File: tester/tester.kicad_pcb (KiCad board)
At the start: 4 copper layers, 150 x 120 mm, 139 parts, among them J101 X1, J102 X3, J103 X2, J201 PWR, J202 SWD, J306 DISP, J307 SD-Card, J401 USB_B_Micro, Q201 SI2301CDS-T1-GE3, SW201 Reset, SW301 SW_Push, SW302 SW_Push, SW303 SW_Push, SW304 SW_Push, SW305 SW_Push, U101 PCA9539xPW, U102 PCA9539xPW, U201 AMS1117-3.3, U202 STM32F103C8Tx, U203 M24C64-RMN, U204 M24C64-RMN, U401 USBLC6-2SC6, U402 XC6206P332MR, U403 CH340N, Y201 8MHz, Y202 32k

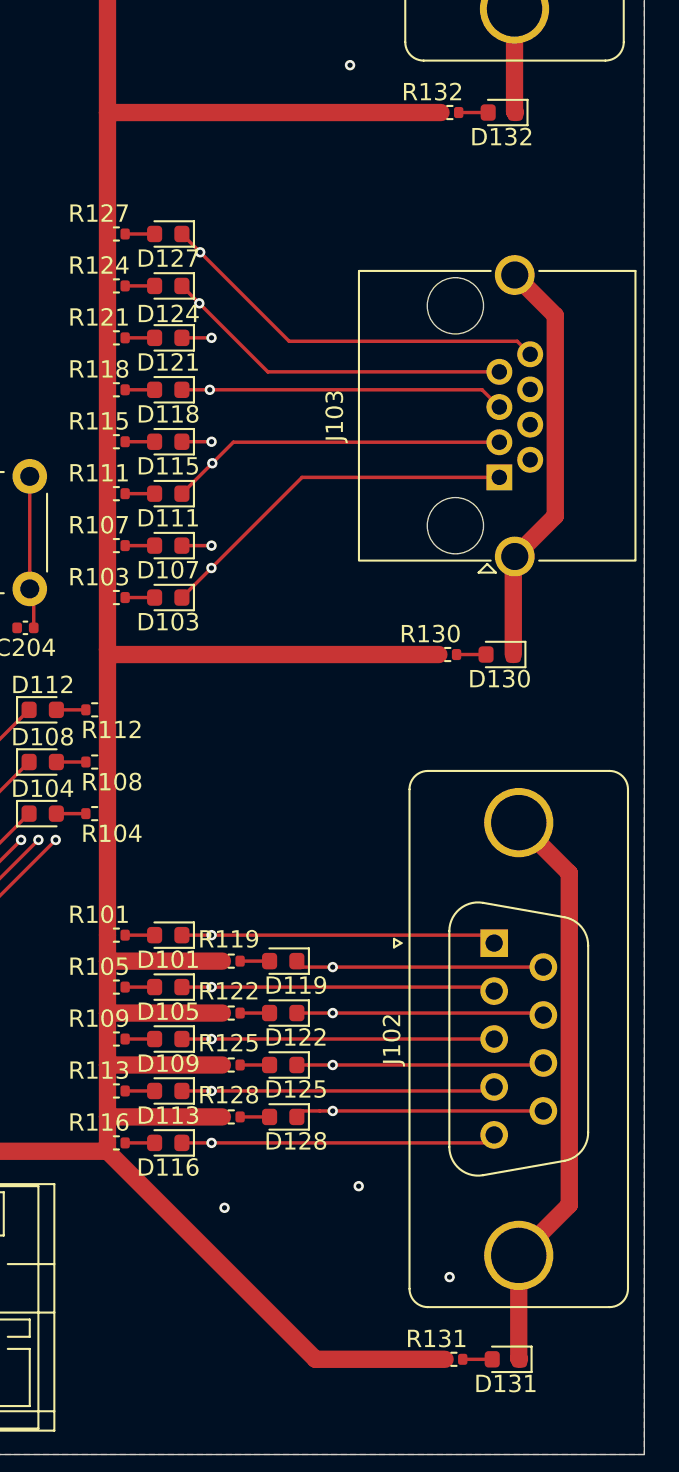
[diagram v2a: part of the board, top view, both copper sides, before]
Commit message: Rework RJ45 connector
Signed-off-by: Benedikt Spranger <b.spranger@linutronix.de>
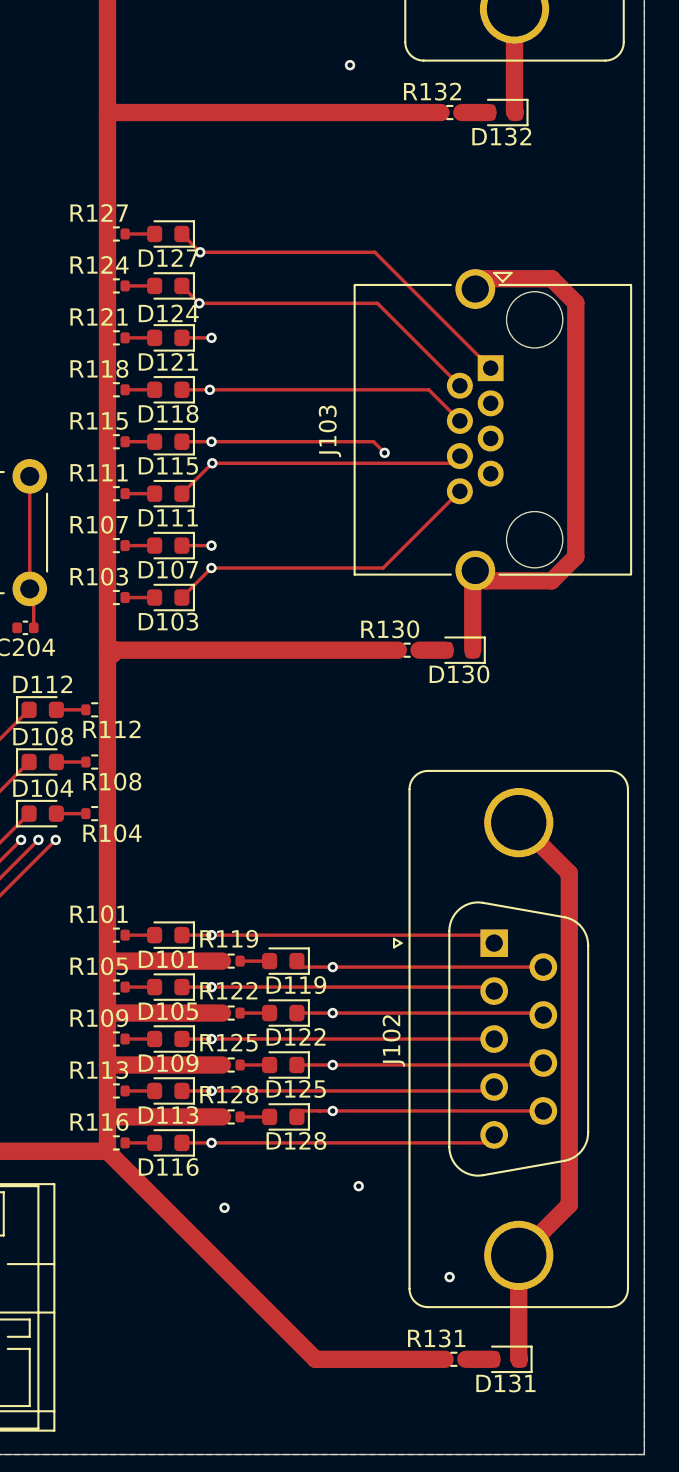
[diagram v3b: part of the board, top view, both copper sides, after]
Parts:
- moved J103 6.33 mm to (256.1, 82.2), turned to -90 degrees
- moved D130 2.36 mm to (254.3, 98.5)
- moved R130 2.36 mm to (251.3, 98.5)
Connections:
- D103 pad 1: /R1 -> /R8
- D107 pad 1: /R2 -> /R7
- D111 pad 1: /R3 -> /R6
- D115 pad 1: /R4 -> /R5
- D118 pad 1: /R5 -> /R4
- D121 pad 1: /R6 -> /R3
- D124 pad 1: /R7 -> /R2
- D127 pad 1: /R8 -> /R1
- U101 pad 13: /R1 -> /R8
- U101 pad 14: /R2 -> /R7
- U101 pad 15: /R3 -> /R6
- U101 pad 16: /R4 -> /R5
- U101 pad 17: /R5 -> /R4
- U101 pad 18: /R6 -> /R3
- U101 pad 19: /R7 -> /R2
- U101 pad 20: /R8 -> /R1
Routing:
- net /R2: track 57.3 -> 41.0 mm
- net /R1: track 56.5 -> 41.5 mm
- net /R4: track 54.7 -> 43.4 mm
- net /R7: track 43.0 -> 54.0 mm
- net /R8: track 43.4 -> 53.9 mm
- net /R5: track 45.4 -> 52.7 mm, vias 2 -> 3
- net /RSH: track 67.1 -> 73.3 mm
- net /R6: track 49.3 -> 46.8 mm
- net +5V: track 236.6 -> 234.4 mm
- net /R3: track 49.4 -> 47.7 mm
- net /MSH: track 109.6 -> 108.3 mm

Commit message: Fix SWD
Signed-off-by: Benedikt Spranger <b.spranger@linutronix.de>
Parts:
- moved C214 0.79 mm to (206.2, 97.0), turned to 0 degrees
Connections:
- U202 pad 25: unconnected-(U202-PB12-Pad25) -> /MCU/~{RST1}
- U202 pad 34: /MCU/~{RST1} -> /MCU/SYS_SWDIO
- U202 pad 38: /MCU/SYS_SWDIO -> unconnected-(U202-PA15-Pad38)
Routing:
- net /MCU/~{RST1}: track 40.9 -> 45.4 mm
- net /MCU/SYS_SWDIO: track 17.0 -> 14.1 mm
- net /MCU/SYS_SWCLK: track 12.5 -> 14.1 mm
- net /MCU/SPI2_MISO: track 100.1 -> 98.5 mm
- net +3V3: track 70.8 -> 71.4 mm
- net /R6: track 46.8 -> 46.2 mm

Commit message: Add missing I2C pullups
Signed-off-by: Benedikt Spranger <b.spranger@linutronix.de>
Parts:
- added R207: 4k7, Resistor_SMD:R_0402_1005Metric, F.Cu at (205.0, 115.5)
- added R208: 4k7, Resistor_SMD:R_0402_1005Metric, F.Cu at (203.8, 115.5)
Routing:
- net /MCU/I2C2_SCL: track 13.0 -> 18.6 mm
- net /MCU/I2C2_SDA: track 13.0 -> 14.8 mm
- net +3V3: track 71.4 -> 73.2 mm, vias 11 -> 12

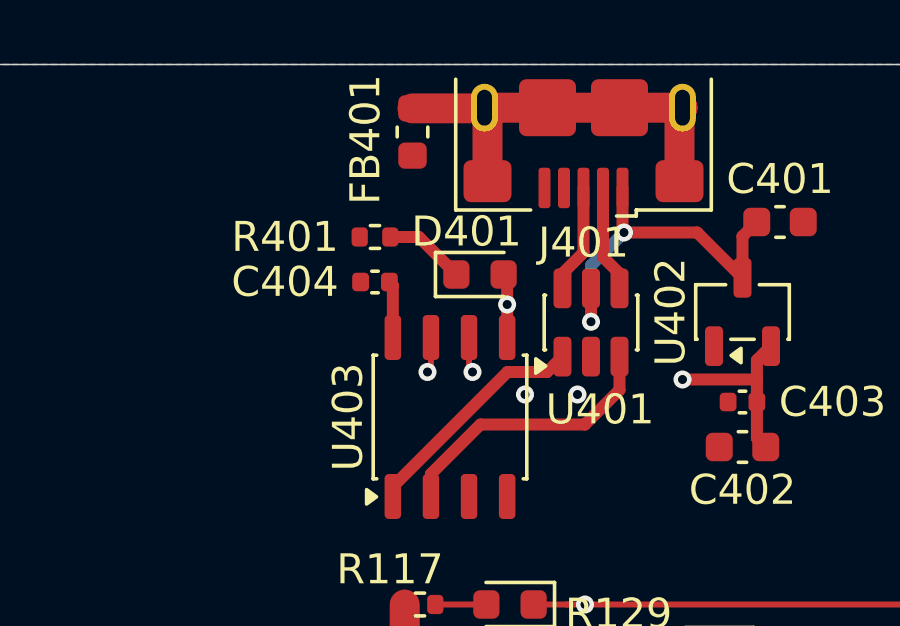
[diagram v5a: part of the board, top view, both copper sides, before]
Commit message: Enable CH340N 3.3V operation
Signed-off-by: Benedikt Spranger <b.spranger@linutronix.de>
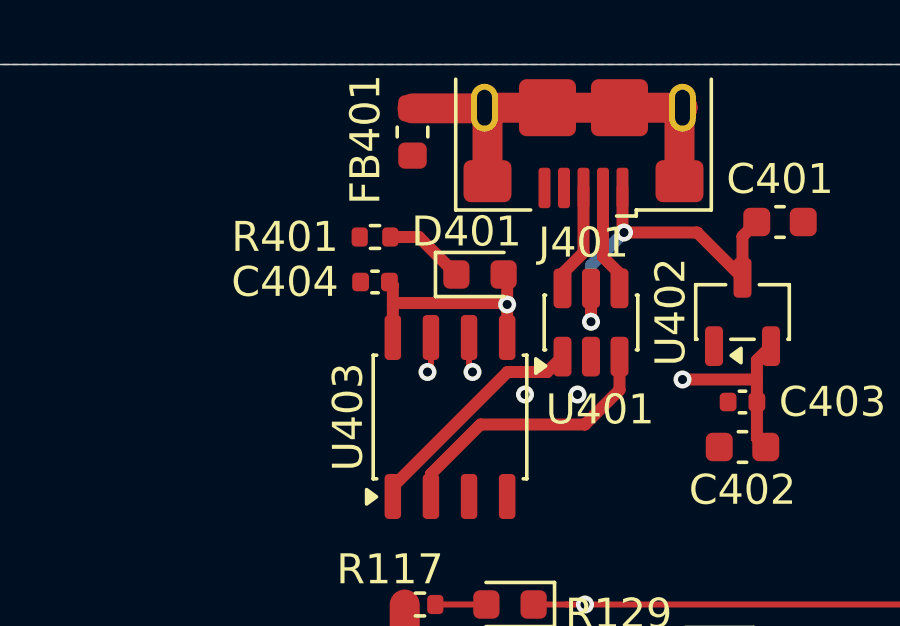
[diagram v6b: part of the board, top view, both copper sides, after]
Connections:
- C404 pad 1: Net-(U403-V3) -> Net-(D401-A)
- U403 pad 8: Net-(U403-V3) -> Net-(D401-A)
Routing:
- net Net-(D401-A): track 15.0 -> 20.8 mm
- net Net-(U403-V3): track 1.90 -> 0.00 mm
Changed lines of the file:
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@@
 			(layers "F.Cu" "F.Mask" "F.Paste")
 			(roundrect_rratio 0.25)
-			(net "Net-(U403-V3)")
+			(net "Net-(D401-A)")
 			(pintype "passive")
 		)
@@
 			(layers "F.Cu" "F.Mask" "F.Paste")
 			(roundrect_rratio 0.25)
-			(net "Net-(U403-V3)")
+			(net "Net-(D401-A)")
 			(pinfunction "V3_8")
 			(pintype "passive")
@@
 	)
 	(segment
+		(start 233.595 32.365)
+		(end 233.48 32.25)
+		(width 0.4)
+		(layer "F.Cu")
+		(net "Net-(D401-A)")
+	)
+	(segment
 		(start 245.73 36.25)
 		(end 245.73 37.455)
@@
 	)
 	(segment
+		(start 233.595 34.1)
+		(end 233.595 33)
+		(width 0.4)
+		(layer "F.Cu")
+		(net "Net-(D401-A)")
+	)
+	(segment
 		(start 245.73 35.5)
 		(end 245.73 34.8575)
@@
 	)
 	(segment
+		(start 233.595 33)
+		(end 233.595 32.365)
+		(width 0.4)
+		(layer "F.Cu")
+		(net "Net-(D401-A)")
+	)
+	(segment
+		(start 233.645 32.95)
+		(end 233.595 33)
+		(width 0.4)
+		(layer "F.Cu")
+		(net "Net-(D401-A)")
+	)
+	(segment
 		(start 245.73 37.455)
 		(end 246.025 37.75)
@@
 	)
 	(segment
+		(start 237.405 33)
+		(end 237.355 32.95)
+		(width 0.4)
+		(layer "F.Cu")
+		(net "Net-(D401-A)")
+	)
+	(segment
 		(start 237.405 34.1)
 		(end 237.405 33)
@@
 		(net "Net-(D401-A)")
 	)
+	(segment
+		(start 237.355 32.95)
+		(end 233.645 32.95)
+		(width 0.4)
+		(layer "F.Cu")
+		(net "Net-(D401-A)")
+	)
 	(via
 		(at 237.405 33)
@@
 	)
 	(segment
+		(start 205 116.055)
+		(end 203.255 117.8)
+		(width 0.2)
+		(layer "F.Cu")
+		(net "/MCU/I2C2_SCL")
+	)
+	(segment
+		(start 201.25 104.1625)
+		(end 201.25 108.41)
+		(width 0.2)
+		(layer "F.Cu")
+		(net "/MCU/I2C2_SCL")
+	)
+	(segment
+		(start 200.885 116.870552)
+		(end 200.885 116.525)
+		(width 0.2)
+		(layer "F.Cu")
+		(net "/MCU/I2C2_SCL")
+	)
+	(segment
+		(start 203.255 117.8)
+		(end 201.814448 117.8)
+		(width 0.2)
+		(layer "F.Cu")
+		(net "/MCU/I2C2_SCL")
+	)
+	(segment
+		(start 201.814448 117.8)
+		(end 200.885 116.870552)
+		(width 0.2)
+		(layer "F.Cu")
+		(net "/MCU/I2C2_SCL")
+	)
+	(segment
+		(start 200.25 109.41)
+		(end 200.25 115.89)
+		(width 0.2)
+		(layer "F.Cu")
+		(net "/MCU/I2C2_SCL")
+	)
+	(segment
+		(start 201.25 108.41)
+		(end 200.885 108.775)
+		(width 0.2)
+		(layer "F.Cu")
+		(net "/MCU/I2C2_SCL")
+	)
+	(segment
+		(start 200.885 108.775)
+		(end 200.25 109.41)
+		(width 0.2)
+		(layer "F.Cu")
+		(net "/MCU/I2C2_SCL")
+	)
+	(segment
+		(start 200.25 115.89)
+		(end 200.885 116.525)
+		(width 0.2)
+		(layer "F.Cu")
+		(net "/MCU/I2C2_SCL")
+	)
+	(segment
 		(start 224.425 115.425)
 		(end 225 116)
@@
 	)
 	(segment
+		(start 201.75 108.37)
+		(end 202.155 108.775)
+		(width 0.2)
+		(layer "F.Cu")
+		(net "/MCU/I2C2_SDA")
+	)
+	(segment
+		(start 201.75 104.1625)
+		(end 201.75 108.37)
+		(width 0.2)
+		(layer "F.Cu")
+		(net "/MCU/I2C2_SDA")
+	)
+	(segment
+		(start 203.295 116.525)
+		(end 203.765 116.055)
+		(width 0.2)
+		(layer "F.Cu")
+		(net "/MCU/I2C2_SDA")
+	)
+	(segment
+		(start 201.555 109.375)
+		(end 201.555 115.925)
+		(width 0.2)
+		(layer "F.Cu")
+		(net "/MCU/I2C2_SDA")
+	)
+	(segment
+		(start 201.555 115.925)
+		(end 202.155 116.525)
+		(width 0.2)
+		(layer "F.Cu")
+		(net "/MCU/I2C2_SDA")
+	)
+	(segment
+		(start 202.155 116.525)
+		(end 203.295 116.525)
+		(width 0.2)
+		(layer "F.Cu")
+		(net "/MCU/I2C2_SDA")
+	)
+	(segment
+		(start 202.155 108.775)
+		(end 201.555 109.375)
+		(width 0.2)
+		(layer "F.Cu")
+		(net "/MCU/I2C2_SDA")
+	)
+	(segment
 		(start 221.974999 71.825)
 		(end 222.275 72.125001)
@@
 	)
 	(segment
-		(start 233.595 32.365)
-		(end 233.48 32.25)
-		(width 0.4)
-		(layer "F.Cu")
-		(net "Net-(U403-V3)")
-	)
-	(segment
-		(start 233.595 34.1)
-		(end 233.595 32.365)
-		(width 0.4)
-		(layer "F.Cu")
-		(net "Net-(U403-V3)")
-	)
-	(segment
 		(start 229.73 97.25)
 		(end 229.73 95.23)
@@
 	)
 	(segment
-		(start 201.75 108.37)
-		(end 202.155 108.775)
-		(width 0.2)
-		(layer "F.Cu")
-		(net "/MCU/I2C2_SDA")
-	)
-	(segment
-		(start 201.75 104.1625)
-		(end 201.75 108.37)
-		(width 0.2)
-		(layer "F.Cu")
-		(net "/MCU/I2C2_SDA")
-	)
-	(segment
-		(start 203.295 116.525)
-		(end 203.765 116.055)
-		(width 0.2)
-		(layer "F.Cu")
-		(net "/MCU/I2C2_SDA")
-	)
-	(segment
-		(start 201.555 109.375)
-		(end 201.555 115.925)
-		(width 0.2)
-		(layer "F.Cu")
-		(net "/MCU/I2C2_SDA")
-	)
-	(segment
-		(start 201.555 115.925)
-		(end 202.155 116.525)
-		(width 0.2)
-		(layer "F.Cu")
-		(net "/MCU/I2C2_SDA")
-	)
-	(segment
-		(start 202.155 116.525)
-		(end 203.295 116.525)
-		(width 0.2)
-		(layer "F.Cu")
-		(net "/MCU/I2C2_SDA")
-	)
-	(segment
-		(start 202.155 108.775)
-		(end 201.555 109.375)
-		(width 0.2)
-		(layer "F.Cu")
-		(net "/MCU/I2C2_SDA")
-	)
-	(segment
-		(start 205 116.055)
-		(end 203.255 117.8)
-		(width 0.2)
-		(layer "F.Cu")
-		(net "/MCU/I2C2_SCL")
-	)
-	(segment
-		(start 201.25 104.1625)
-		(end 201.25 108.41)
-		(width 0.2)
-		(layer "F.Cu")
-		(net "/MCU/I2C2_SCL")
-	)
-	(segment
-		(start 200.885 116.870552)
-		(end 200.885 116.525)
-		(width 0.2)
-		(layer "F.Cu")
-		(net "/MCU/I2C2_SCL")
-	)
-	(segment
-		(start 203.255 117.8)
-		(end 201.814448 117.8)
-		(width 0.2)
-		(layer "F.Cu")
-		(net "/MCU/I2C2_SCL")
-	)
-	(segment
-		(start 201.814448 117.8)
-		(end 200.885 116.870552)
-		(width 0.2)
-		(layer "F.Cu")
-		(net "/MCU/I2C2_SCL")
-	)
-	(segment
-		(start 200.25 109.41)
-		(end 200.25 115.89)
-		(width 0.2)
-		(layer "F.Cu")
-		(net "/MCU/I2C2_SCL")
-	)
-	(segment
-		(start 201.25 108.41)
-		(end 200.885 108.775)
-		(width 0.2)
-		(layer "F.Cu")
-		(net "/MCU/I2C2_SCL")
-	)
-	(segment
-		(start 200.885 108.775)
-		(end 200.25 109.41)
-		(width 0.2)
-		(layer "F.Cu")
-		(net "/MCU/I2C2_SCL")
-	)
-	(segment
-		(start 200.25 115.89)
-		(end 200.885 116.525)
-		(width 0.2)
-		(layer "F.Cu")
-		(net "/MCU/I2C2_SCL")
-	)
-	(segment

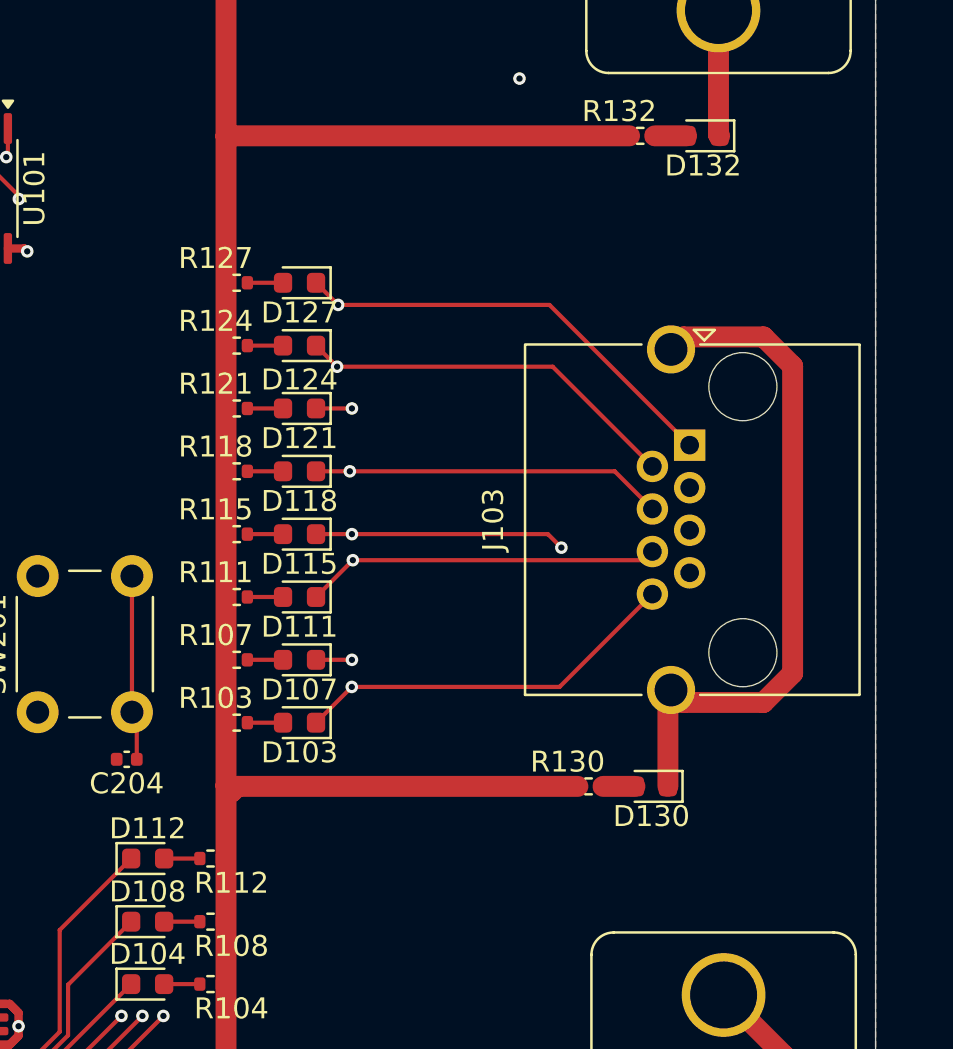
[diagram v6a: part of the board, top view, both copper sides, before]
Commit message: Use RJ45 connector with LEDs
Signed-off-by: Benedikt Spranger <b.spranger@linutronix.de>
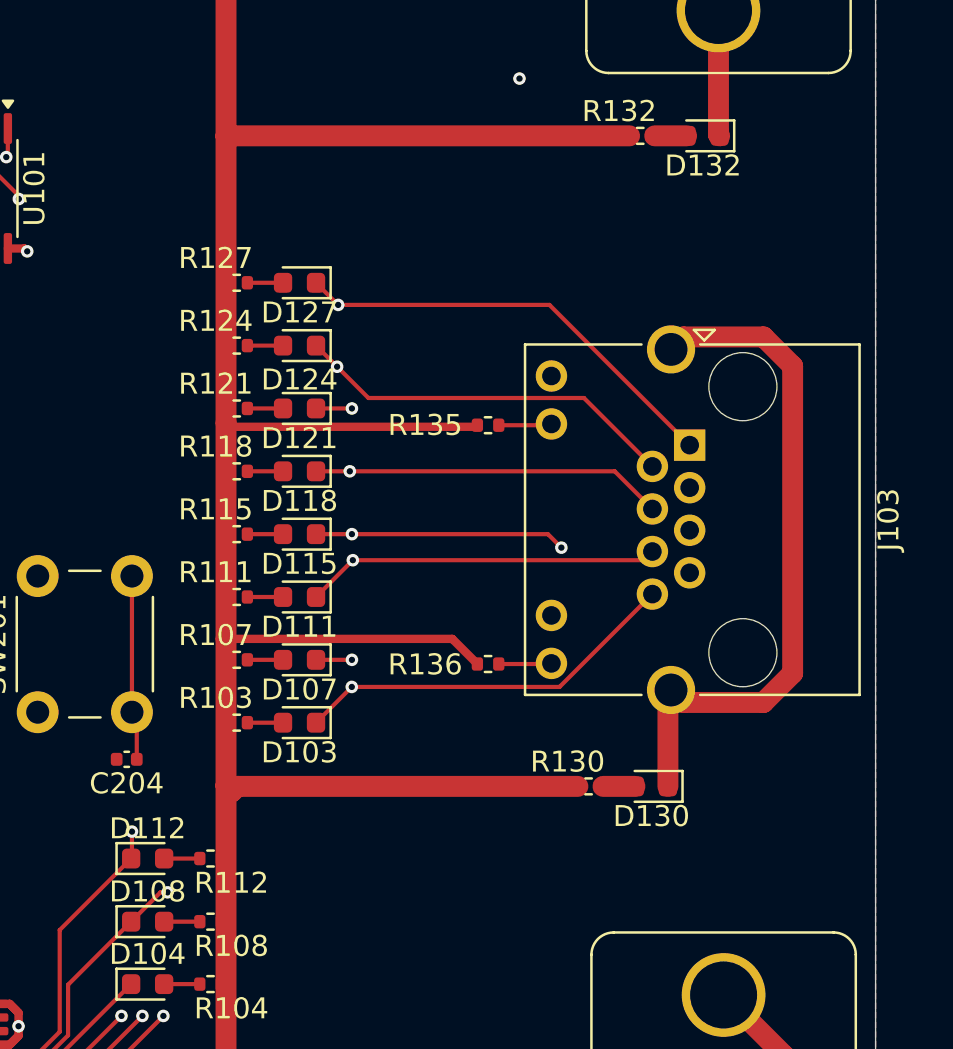
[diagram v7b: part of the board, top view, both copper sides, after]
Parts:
- added R135: 1k, Resistor_SMD:R_0402_1005Metric, F.Cu at (246.5, 81.3)
- added R136: 1k, Resistor_SMD:R_0402_1005Metric, F.Cu at (246.5, 92.7)
- J103: footprint Connector_RJ:RJ45_Amphenol_RJHSE5380 -> Connector_RJ:RJ45_Amphenol_RJHSE538X
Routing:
- net /LED2: track 13.4 -> 44.7 mm, vias 0 -> 1
- net /LED1: track 11.0 -> 37.1 mm, vias 0 -> 1
- net +5V: track 234.4 -> 259.0 mm
- net Net-(J103-Pad10): track 0.00 -> 2.54 mm
- net Net-(J103-Pad12): track 0.00 -> 2.53 mm
